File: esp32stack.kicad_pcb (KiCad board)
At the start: 2 copper layers, 48.1 x 56.4 mm, 30 parts, among them J1 CONN_01X17, J2 CONN_01X16, P1 USB_OTG, Q1 MMBT3904, Q2 MMBT3904, SW1 SWITCH_SPST, SW2 SWITCH_SPST, U1 ESP32-WROOM, U2 NCP1117ST33T3G, U3 CP2102

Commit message: Change condensor position
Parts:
- moved C4 2.57 mm to (162.0, 103.7)
- moved C5 2.54 mm to (162.0, 106.3)
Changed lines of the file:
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@@
     (links 98)
     (no_connects 0)
-    (area 144.826667 61.255 201.30522 121.368)
+    (area 144.826667 52.3291 213.3741 121.368)
     (thickness 1.6)
     (drawings 95)
@@
   )
   (module Capacitors_SMD:C_0603 (layer F.Cu)
-    (at 161.9885 106.299 180)
+    (at 161.9504 103.7336 180)
     (descr "Capacitor SMD 0603, reflow soldering, AVX (see smccp.pdf)")
     (tags "capacitor 0603")
@@
   )
   (module Capacitors_SMD:C_0603 (layer F.Cu)
-    (at 162.0012 103.7336 180)
+    (at 161.9504 106.2736 180)
     (descr "Capacitor SMD 0603, reflow soldering, AVX (see smccp.pdf)")
     (tags "capacitor 0603")

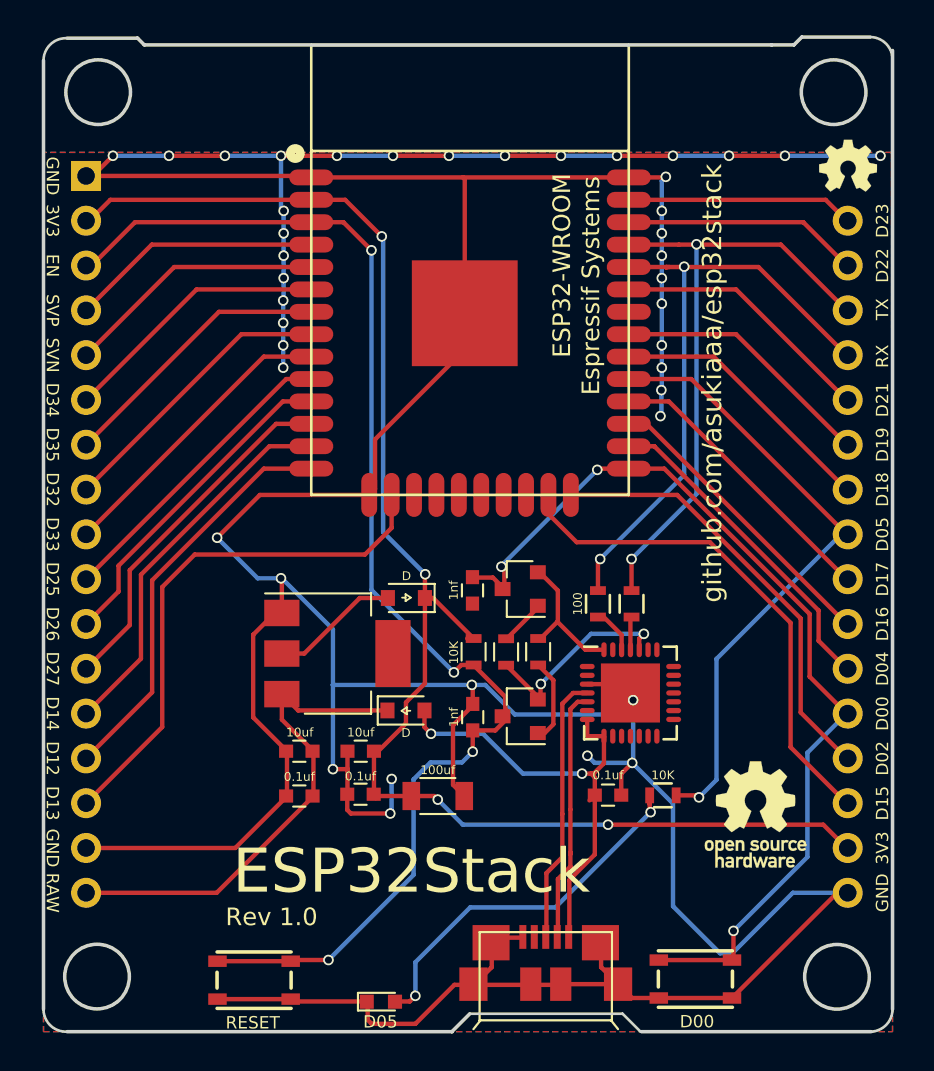
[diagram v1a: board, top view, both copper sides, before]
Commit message: Change pcb layout for rev1.1
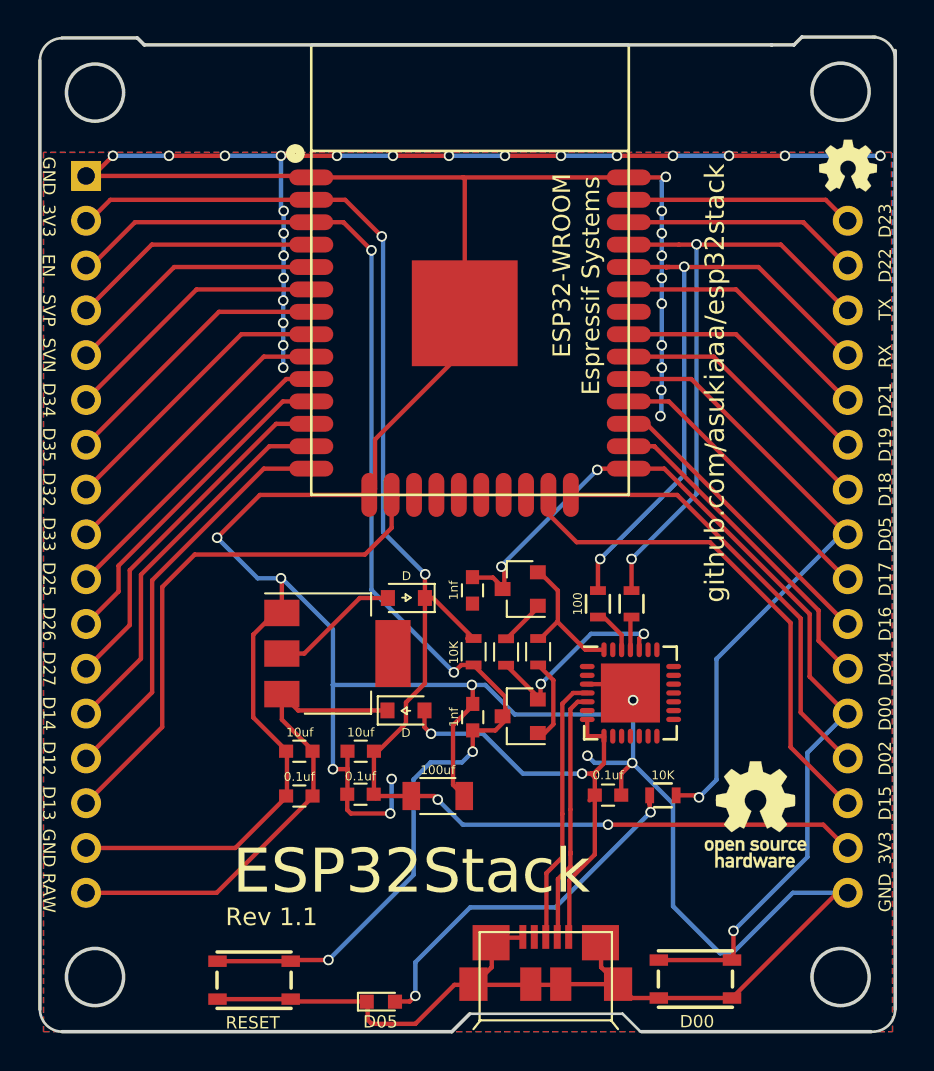
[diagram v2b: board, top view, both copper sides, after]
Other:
- board size 48.1 x 56.4 mm -> 48.5 x 56.4 mm
- board text added: "Rev 1.1"
- board text removed: "Rev 1.0"

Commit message: Change usb connector and led position for rev1.2
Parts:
- moved D3 12.1 mm to (178.7, 117.9)
- moved P1 4.88 mm to (171.0, 118.4)
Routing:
- net Net-(D3-Pad2): track 22.3 -> 13.1 mm, vias 2 -> 0
- net +5V: track 26.6 -> 28.9 mm
- net D+: track 15.3 -> 17.5 mm
- net D-: track 14.5 -> 16.5 mm
- net GND: track 299.9 -> 299.3 mm
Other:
- outline, holes or cut-outs redrawn
- board text added: "Rev 1.2"
- board text removed: "Rev 1.1"
